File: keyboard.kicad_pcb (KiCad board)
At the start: 2 copper layers, 69.1 x 68.1 mm, 77 parts, among them J1 CONN-PALM-FOLD-KB, P1 Keyboard Even, P2 Keyboard Odd, P3 PS2, P4 Palm Serial, P5 ARM debug header, P6 Power, P7 USB_H, Q1 BSS138, Q2 BSS138, Q3 BSS138, SW1 SW_PUSH, U1 CONN-X220-KB, U2 MCP1700-2202E/TT, U3 EFM32G222F32, X1 CRYSTAL

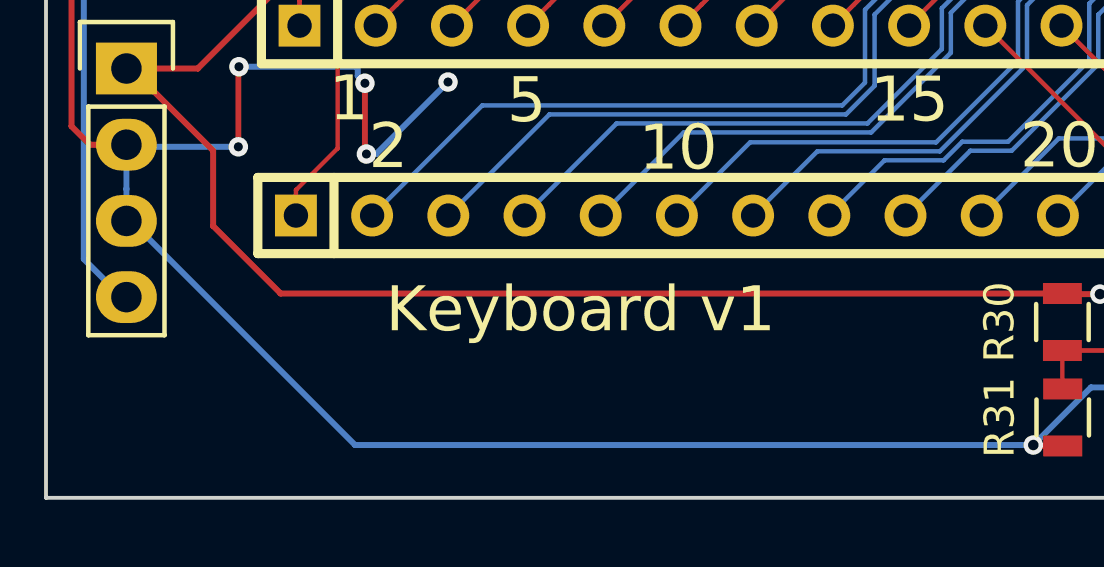
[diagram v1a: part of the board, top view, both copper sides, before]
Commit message: Add open source logo
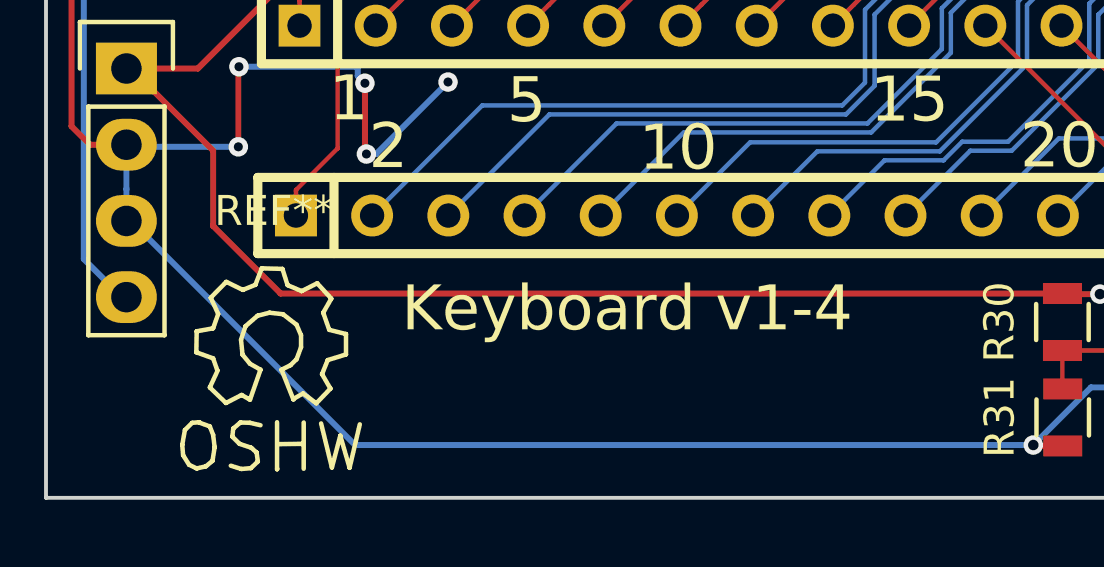
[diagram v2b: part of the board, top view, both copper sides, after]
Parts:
- added REF**: Symbol_OSHW-Logo_SilkScreen, Symbols:Symbol_OSHW-Logo_SilkScreen, F.Cu at (137.5, 105.9)
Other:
- board text added: "Keyboard v1-4"
- board text removed: "Keyboard v1"

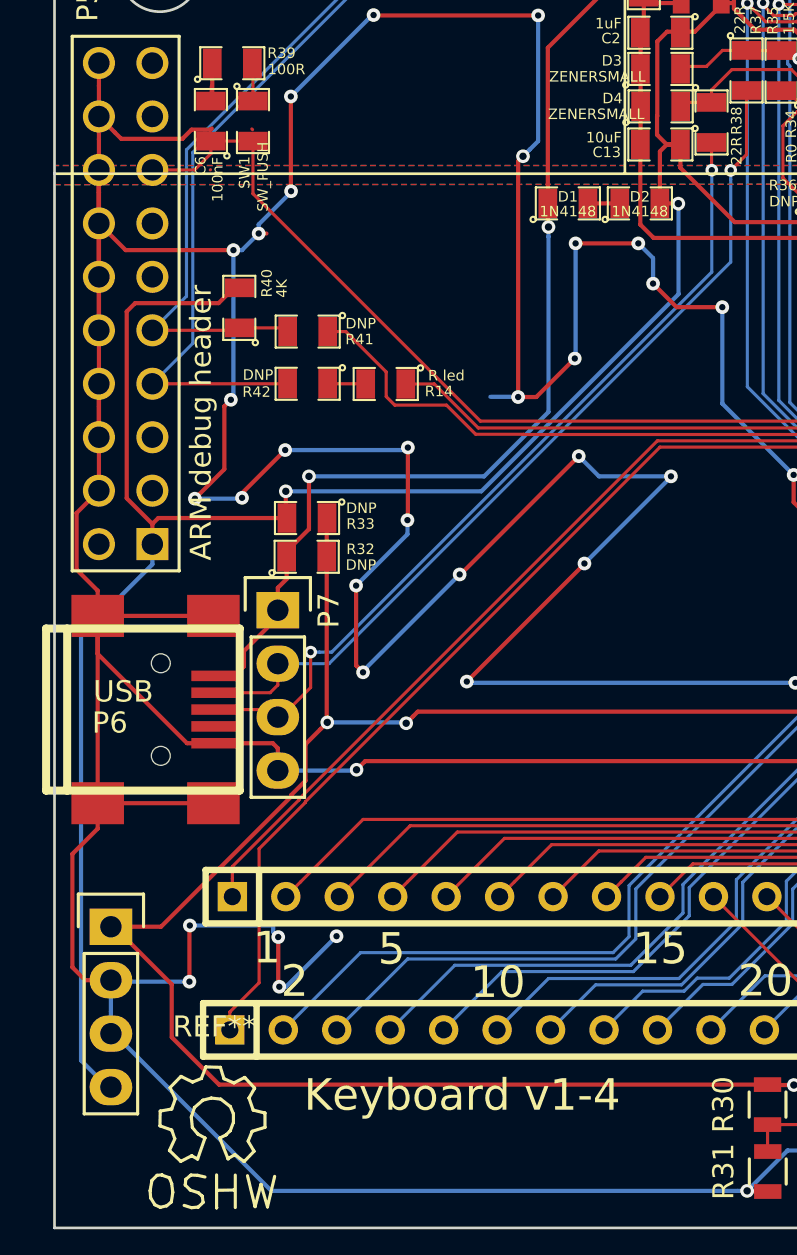
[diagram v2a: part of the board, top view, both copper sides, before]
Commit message: Fix nets crossing - GND with reset
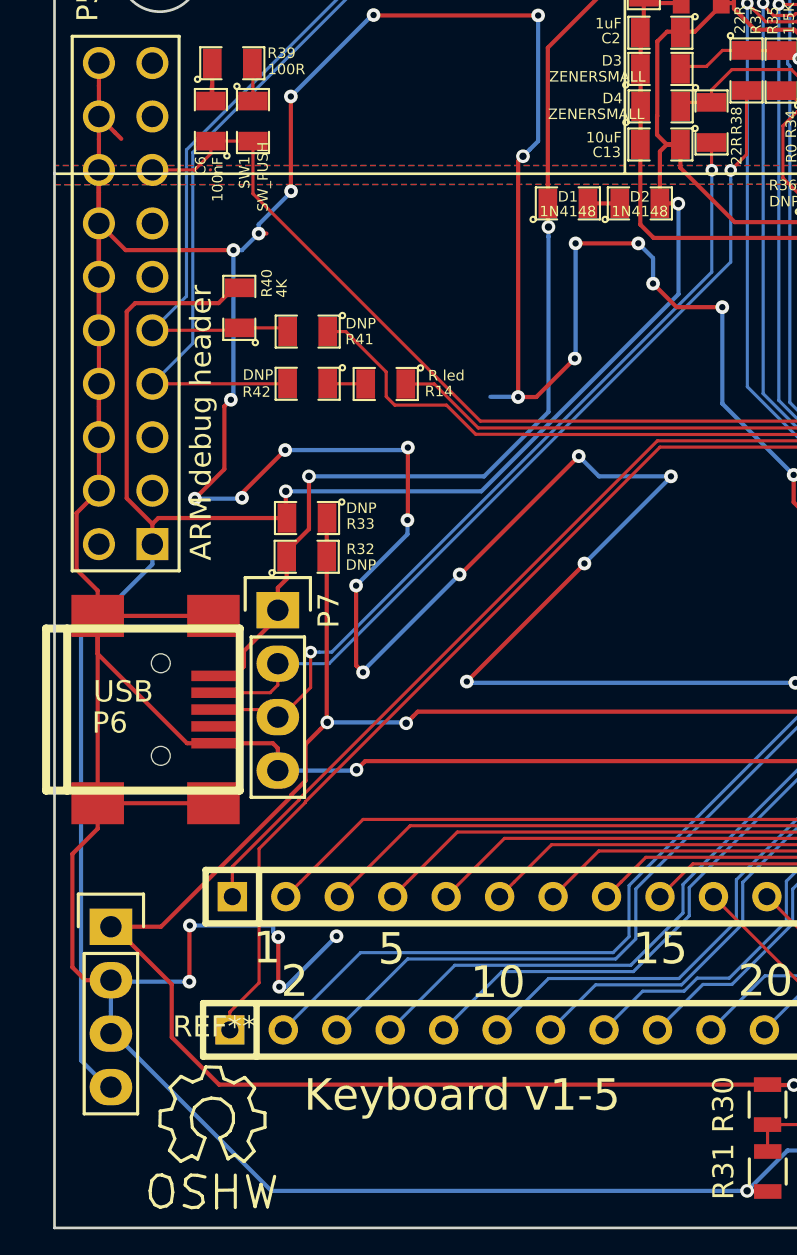
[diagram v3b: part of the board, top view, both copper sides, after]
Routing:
- net GND: track 648.2 -> 643.7 mm
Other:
- board text added: "Keyboard v1-5"
- board text removed: "Keyboard v1-4"

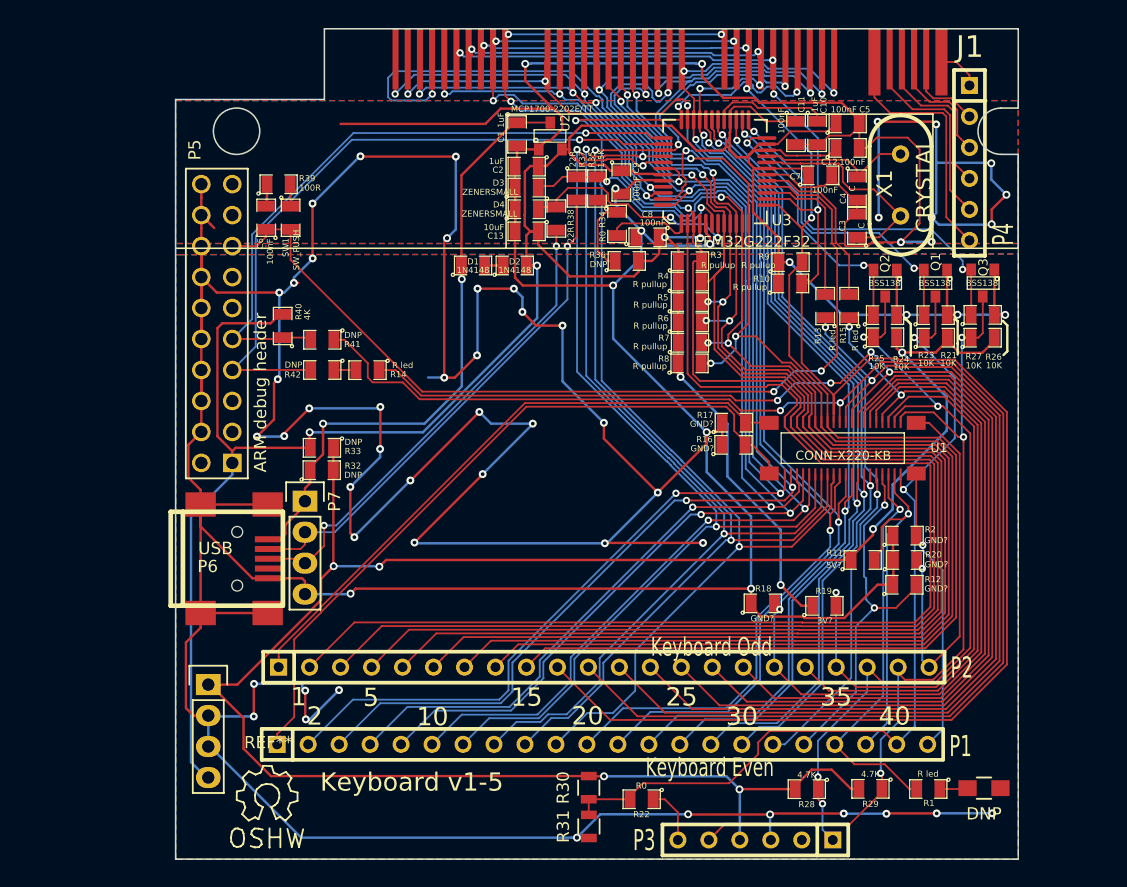
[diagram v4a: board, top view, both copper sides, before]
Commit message: Update USB footprint, clean up more minor PCB warts
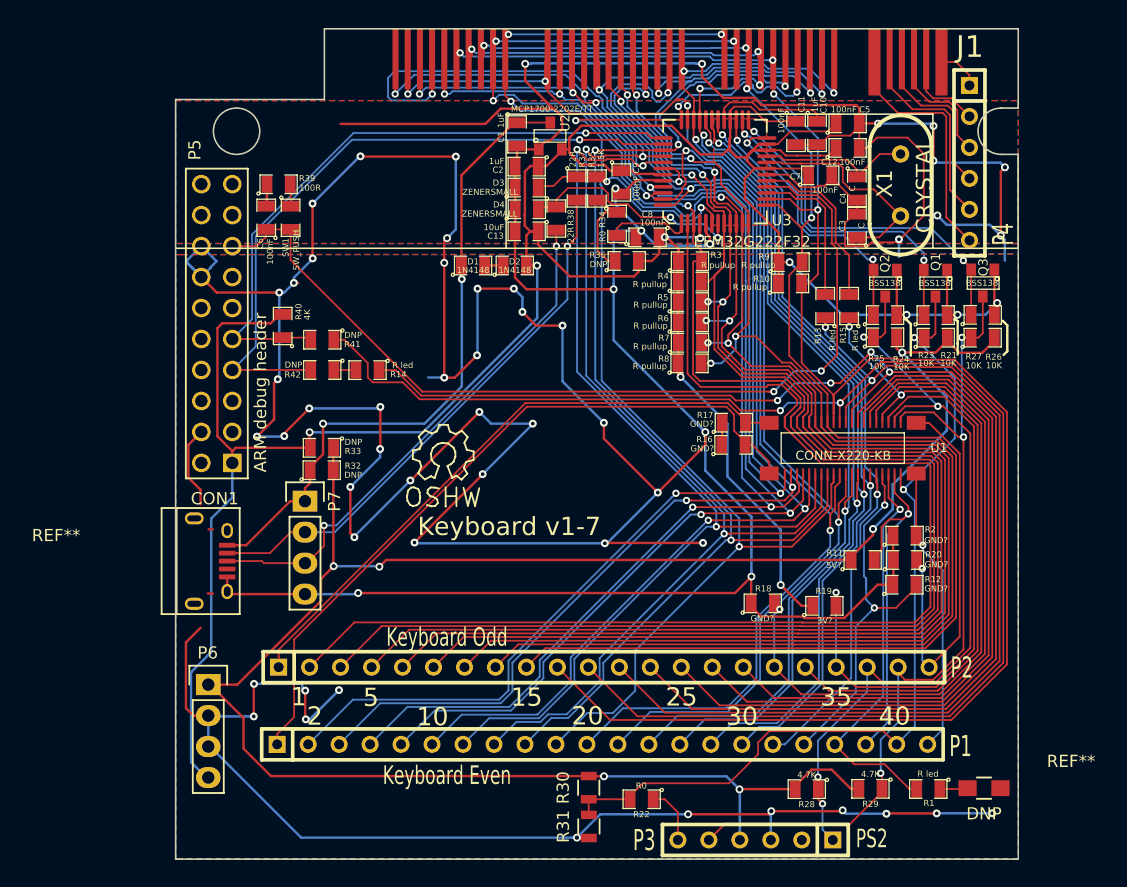
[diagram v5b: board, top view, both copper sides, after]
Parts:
- removed USB: USB-MICRO-B, USB_MINI_B
- added CON1: USB-MICRO-B, Connect:USB_Micro-B, F.Cu at (134.2, 85.3)
- moved REF** 31.5 mm to (151.9, 78.0)
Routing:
- net GND: track 643.7 -> 578.5 mm, vias 60 -> 59
- net Net-(CON1-Pad3): track 39.6 -> 43.0 mm
- net /keyboard-power/VBUS: track 50.9 -> 54.2 mm
- net Net-(CON1-Pad2): track 42.0 -> 45.0 mm
- net +3V3: track 255.3 -> 256.5 mm
- net /keyboard-efm32/ps2_reset: track 25.9 -> 26.7 mm
- net (no net): track 0.01 -> 0.75 mm
- net row2: track 109.8 -> 109.2 mm
- added copper zone on F.Cu, net +3V3
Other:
- board text added: "Keyboard v1-7"
- board text removed: "Keyboard v1-5"
